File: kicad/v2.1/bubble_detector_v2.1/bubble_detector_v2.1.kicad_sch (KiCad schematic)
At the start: 7 parts, among them J1 Power, J2 Digital/PWM, J3 Analog, J4 Digital/PWM, U1 HC-SR04

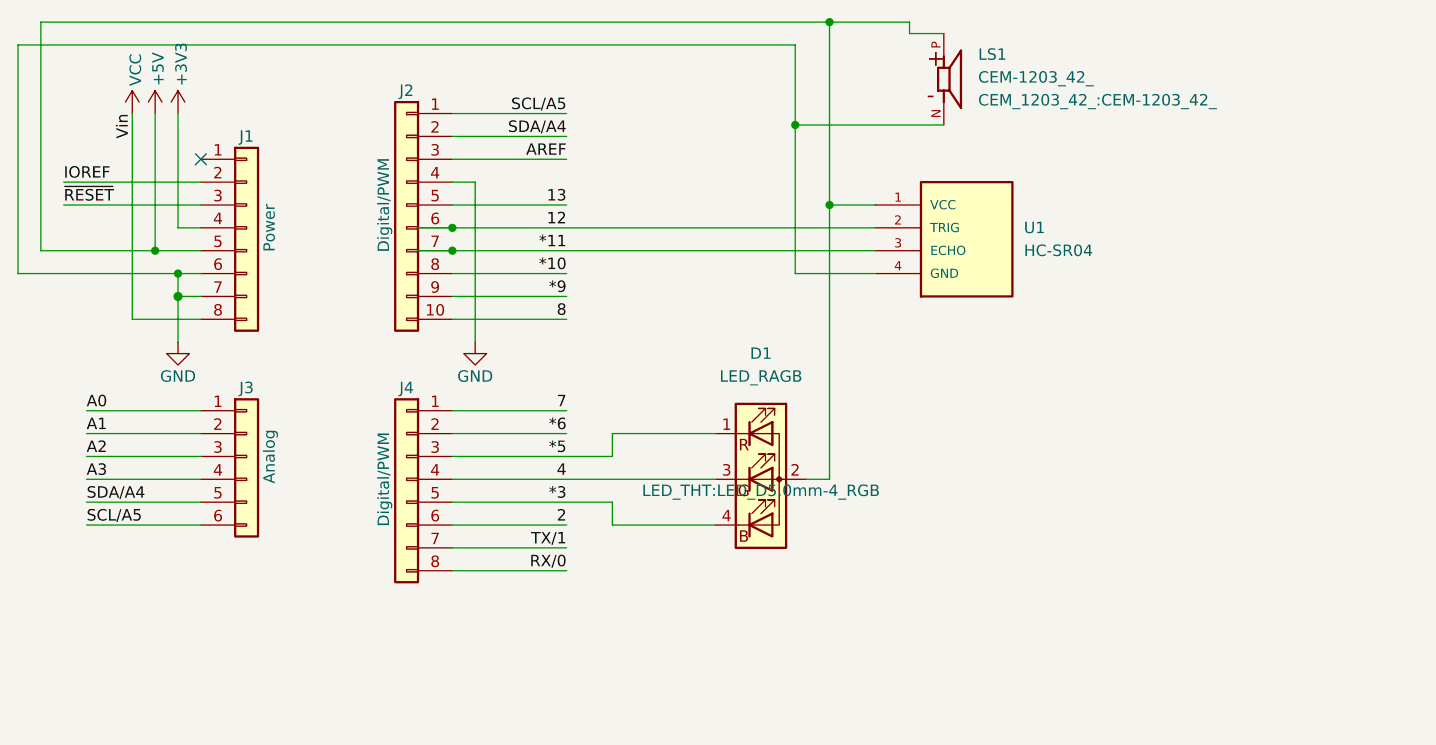
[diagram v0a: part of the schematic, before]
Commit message: adding arduino library
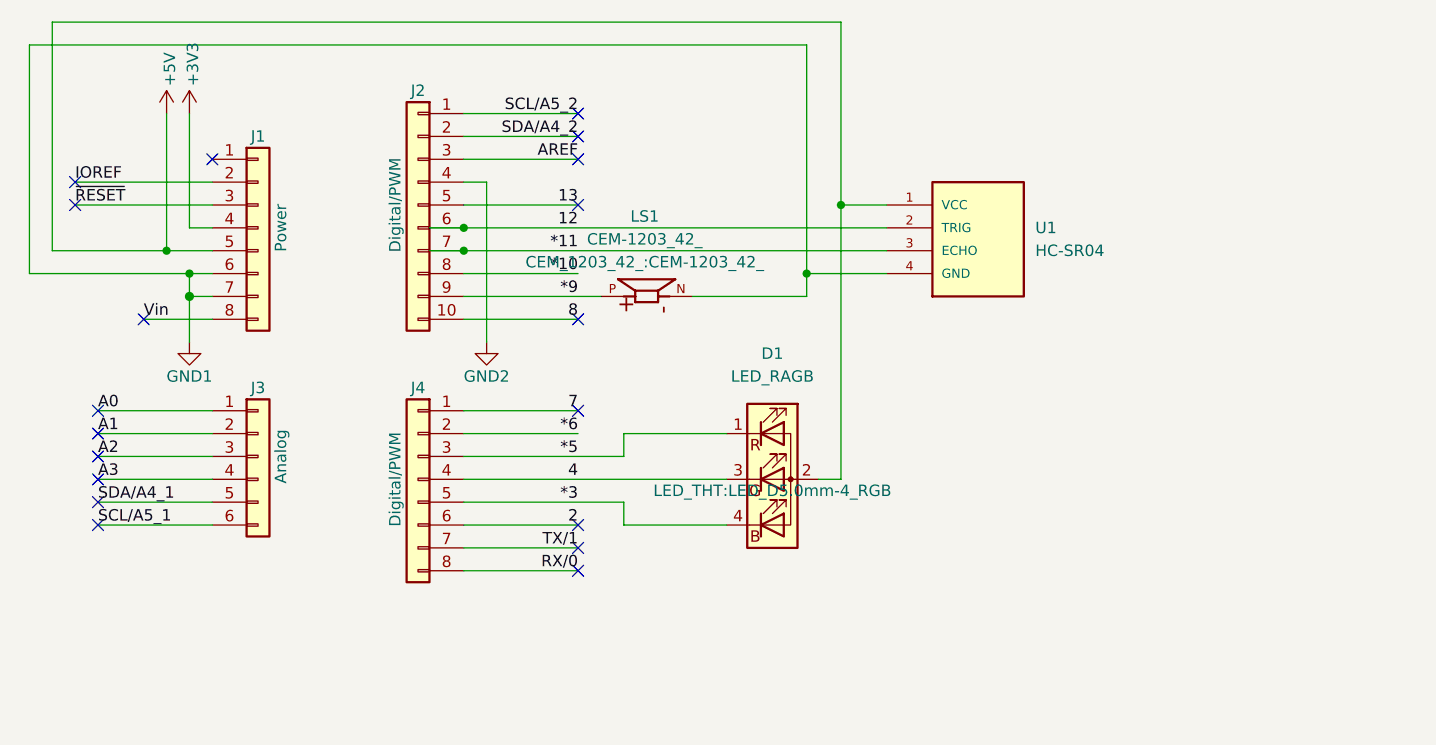
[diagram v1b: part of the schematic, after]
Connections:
- net *9: now also LS1.P
- net +5V: no longer LS1.P
- net GND renamed GND1
- net GND1: no longer J2.4 (Pin_4)
- net SCL/A5 renamed SCL/A5_1
- net SCL/A5_1: no longer J2.1 (Pin_1)
- net SDA/A4 renamed SDA/A4_1
- net SDA/A4_1: no longer J2.2 (Pin_2)
- net VCC renamed Vin
- new net GND2: J2.4 (Pin_4)
- new net SCL/A5_2: J2.1 (Pin_1)
- new net SDA/A4_2: J2.2 (Pin_2)
- no-connect marks 1 -> 19
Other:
- company: (none) -> Warren Tech - Jeffco Public Schools
- title: (none) -> H.I.V.A. Hunch Bubble Detector
- moved on the sheet: D1, J1, J2, J3, J4, LS1, U1

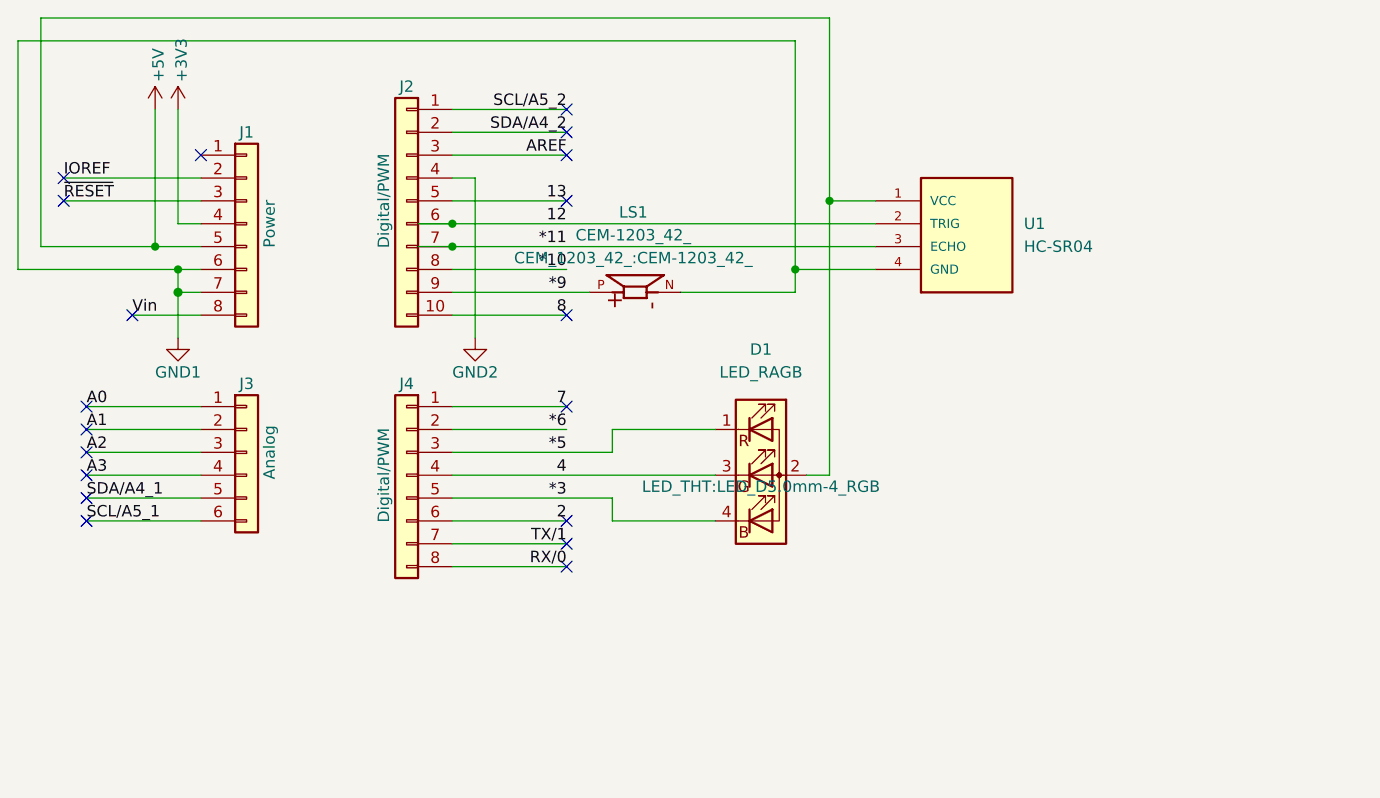
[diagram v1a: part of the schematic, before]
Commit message: added servo and am working on schematic
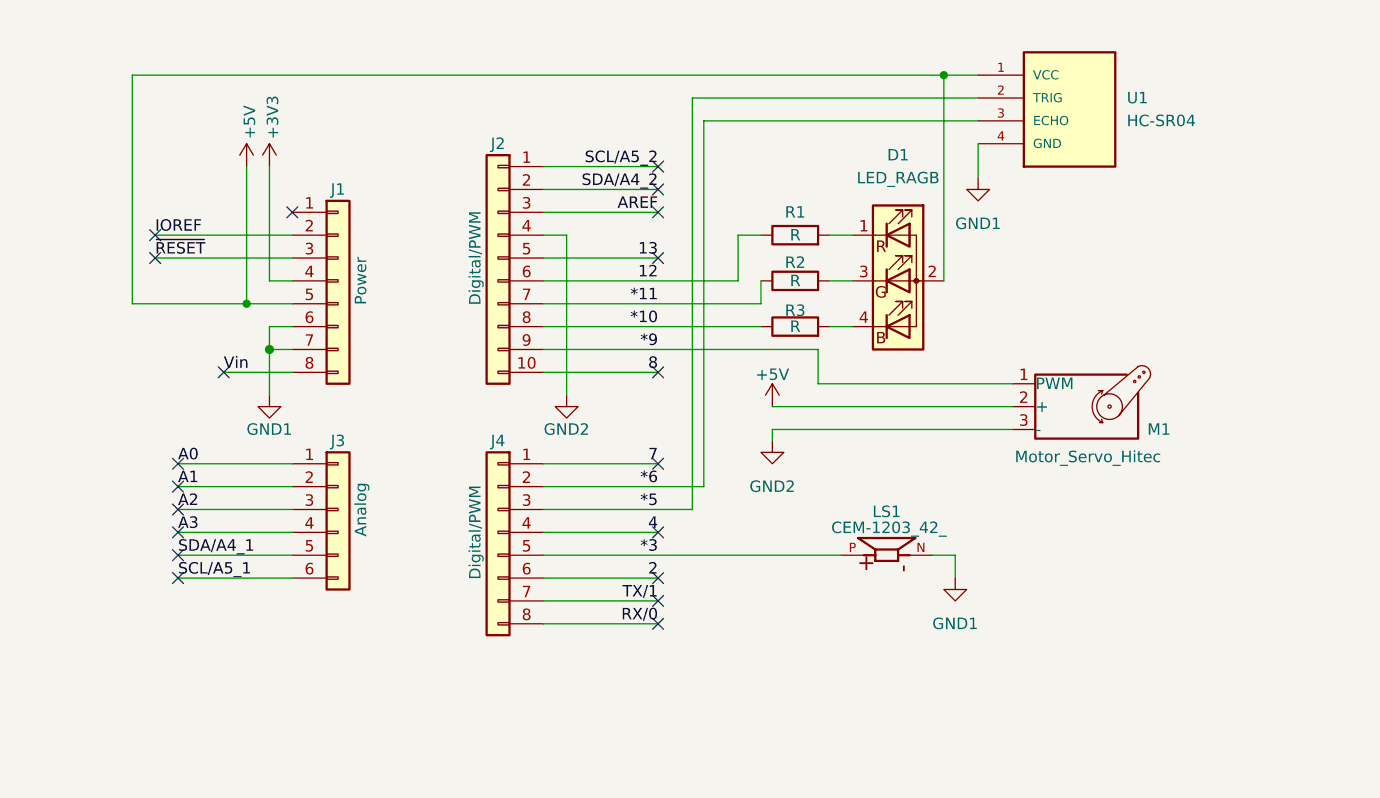
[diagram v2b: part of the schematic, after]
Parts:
- added M1: Motor_Servo_Hitec, Connector_PinHeader_2.54mm:PinHeader_1x03_P2.54mm_Vertical, symbol Motor:Motor_Servo_Hitec
- added R1, R2, R3: R, Resistor_THT:R_Axial_DIN0309_L9.0mm_D3.2mm_P12.70mm_Horizontal, symbol Device:R
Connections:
- net *10: now also R3.1
- net *11: now also R2.1; no longer U1.3 (ECHO)
- net *3: now also LS1.P; no longer D1.4 (BK)
- net *5: now also U1.2 (TRIG); no longer D1.1 (RK)
- net *6: now also U1.3 (ECHO)
- net *9: now also M1.1 (PWM); no longer LS1.P
- net +5V: now also M1.2 (+)
- net 12: now also R1.1; no longer U1.2 (TRIG)
- net 4: no longer D1.3 (GK)
- net GND2: now also M1.3 (-)
- new net: D1.1 (RK), R1.2
- new net: D1.3 (GK), R2.2
- new net: D1.4 (BK), R3.2
- no-connect marks 19 -> 20
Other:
- moved on the sheet: D1, J1, J2, J3, J4, LS1, U1

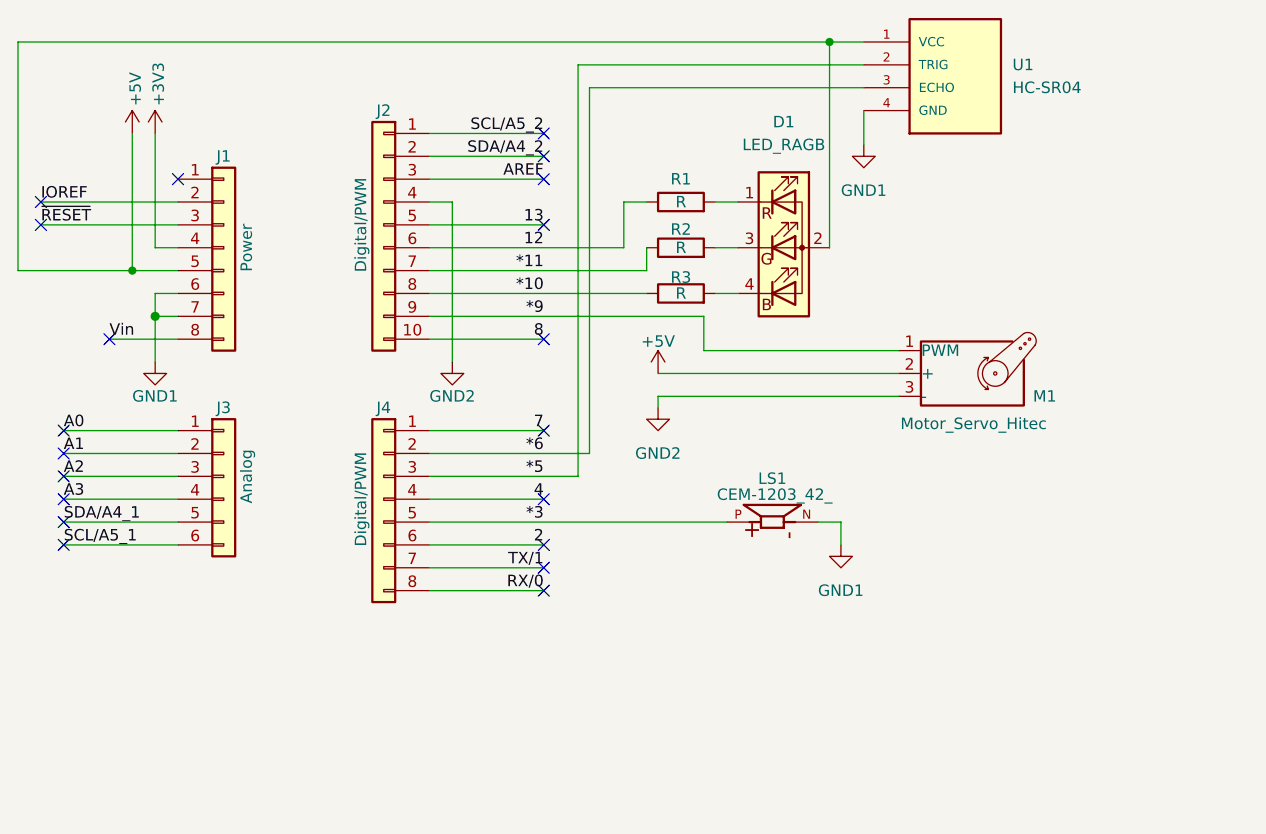
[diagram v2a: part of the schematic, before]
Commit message: Added all componenets, generated gerbers
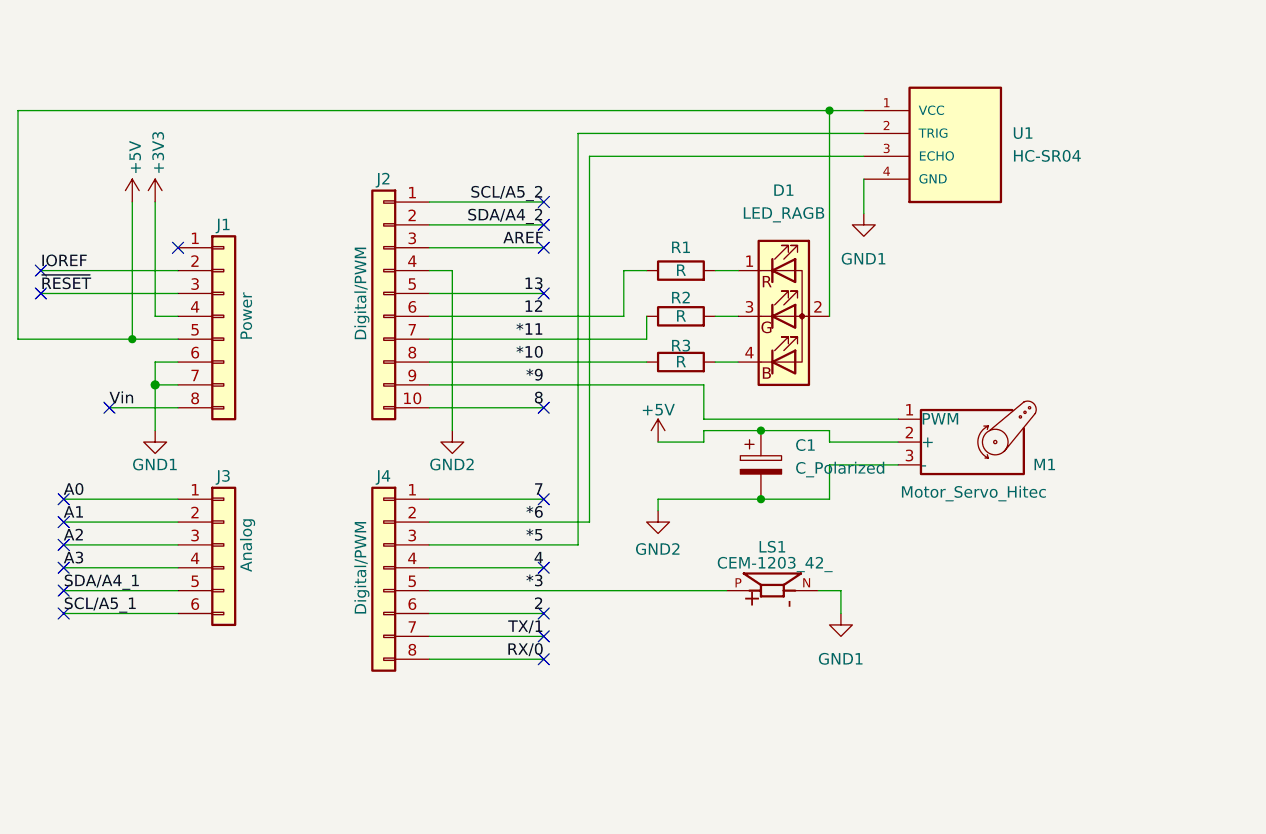
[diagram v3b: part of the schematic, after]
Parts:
- added C1: C_Polarized, Capacitor_THT:CP_Radial_D5.0mm_P2.50mm, symbol Device:C_Polarized
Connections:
- net +5V: now also C1.1
- net GND2: now also C1.2
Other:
- moved on the sheet: D1, J1, J2, J3, J4, LS1, M1, R1, R2, R3, U1
